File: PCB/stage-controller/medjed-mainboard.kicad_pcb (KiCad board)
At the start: 2 copper layers, 28 parts, among them IC1 TMC429-LI, J1 Barrel_Jack, U1 RP2040

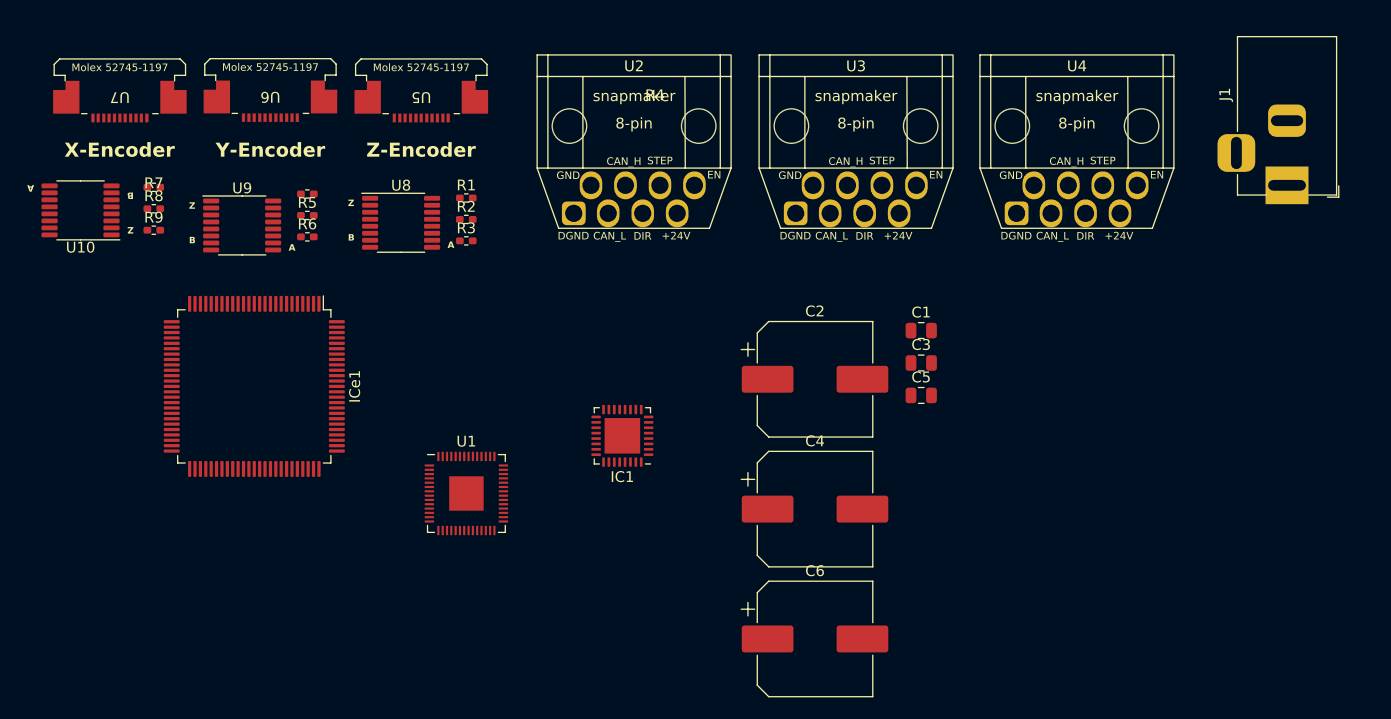
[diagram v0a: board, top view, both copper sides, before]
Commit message: Add initial version stage PCB
Will probably need major revisions as efforts towards TMC4361A will require significant changes.
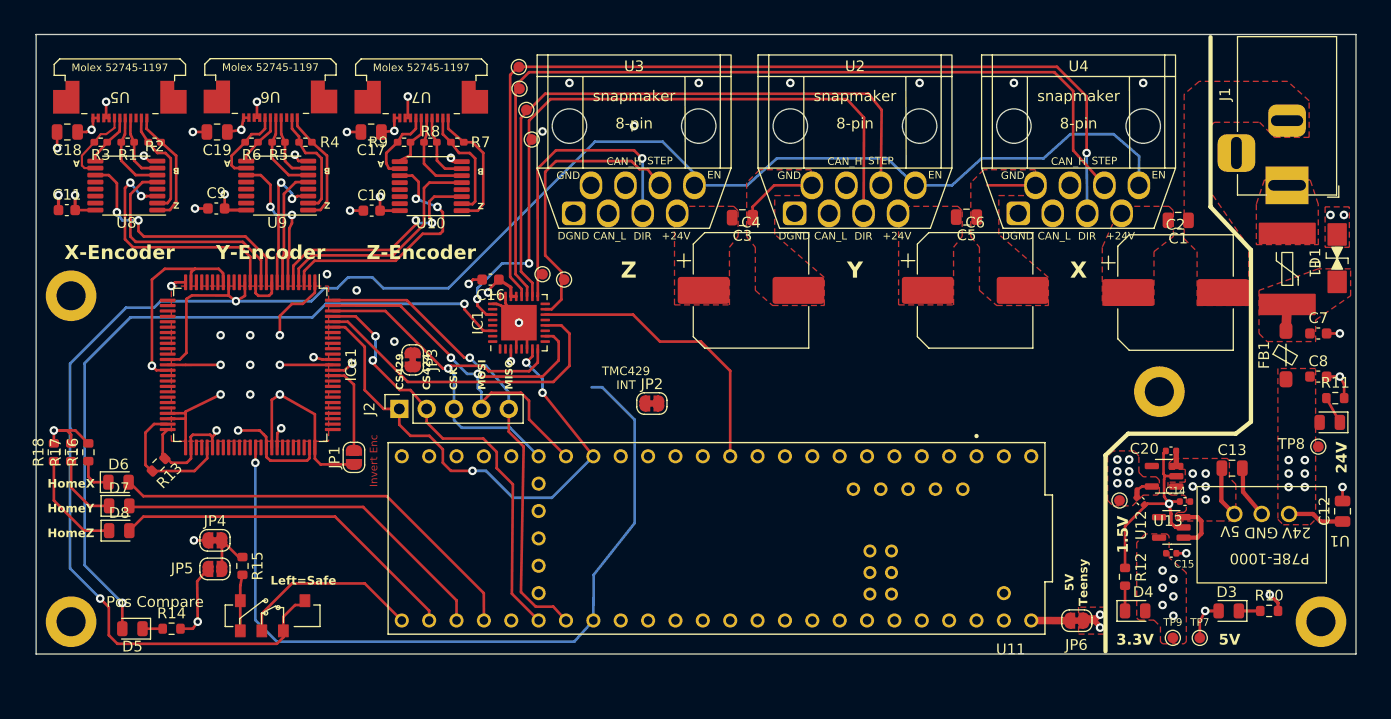
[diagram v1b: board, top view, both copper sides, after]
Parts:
- added ?: , , F.Cu at (135.5, 73.8)
- added ?: , , F.Cu at (120.5, 52.4)
- added ?: , , F.Cu at (19.5, 73.8)
- added C10: 100nF, Capacitor_SMD:C_0603_1608Metric, F.Cu at (47.4, 35.6)
- added C11: 100nF, Capacitor_SMD:C_0603_1608Metric, F.Cu at (19.1, 35.6)
- added C12: 10uF, Capacitor_SMD:C_0805_2012Metric, F.Cu at (137.5, 63.5)
- added C13: 22uF, Capacitor_SMD:C_0805_2012Metric, F.Cu at (127.2, 59.5)
- added C14: 1uF, Capacitor_SMD:C_0402_1005Metric, F.Cu at (122.9, 62.6)
- added C15: 1uF, Capacitor_SMD:C_0402_1005Metric, F.Cu at (121.6, 67.4)
- added C16: 100nF, Capacitor_SMD:C_0603_1608Metric, F.Cu at (58.4, 42.0)
- added C17: 10uF, Capacitor_SMD:C_0805_2012Metric, F.Cu at (47.4, 28.3)
- added C18: 10uF, Capacitor_SMD:C_0805_2012Metric, F.Cu at (19.1, 28.3)
- added C19: 10uF, Capacitor_SMD:C_0805_2012Metric, F.Cu at (33.0, 28.3)
- added C20: 1uF, Capacitor_SMD:C_0402_1005Metric, F.Cu at (121.6, 57.9)
- added C21: 1uF, Capacitor_SMD:C_0402_1005Metric, F.Cu at (118.8, 62.6)
- added C7: 100nF, Capacitor_SMD:C_0603_1608Metric, F.Cu at (135.2, 47.0)
- added C8: 100nF, Capacitor_SMD:C_0603_1608Metric, F.Cu at (135.2, 51.0)
- added C9: 100nF, Capacitor_SMD:C_0603_1608Metric, F.Cu at (33.0, 35.4)
- added D1: SMAJ28CA, medjed-mainboard:SMAJ28CA, F.Cu at (137.0, 40.0)
- added D2: Red, LED_SMD:LED_0805_2012Metric, F.Cu at (136.3, 55.2)
- added D3: Red, LED_SMD:LED_0805_2012Metric, F.Cu at (126.9, 72.8)
- added D4: Red, LED_SMD:LED_0805_2012Metric, F.Cu at (118.2, 72.8)
- added D5: Red, LED_SMD:LED_0805_2012Metric, F.Cu at (25.2, 74.4)
- added D6: Red, LED_SMD:LED_0805_2012Metric, F.Cu at (23.9, 60.8)
- added D7: Red, LED_SMD:LED_0805_2012Metric, F.Cu at (24.0, 63.0)
- added D8: Red, LED_SMD:LED_0805_2012Metric, F.Cu at (24.0, 65.3)
- added F1: SMDC185F/33-2, medjed-mainboard:SMDC185F_33-2, F.Cu at (132.4, 41.0)
- added FB1: FerriteBead, medjed-mainboard:BLM41P600S, F.Cu at (132.2, 49.0)
- added J2: Conn_01x05, Connector_PinSocket_2.54mm:PinSocket_1x05_P2.54mm_Vertical, F.Cu at (50.0, 54.0)
- added JP1: SolderJumper_2_Open, Jumper:SolderJumper-2_P1.3mm_Open_RoundedPad1.0x1.5mm, F.Cu at (45.8, 58.5)
- added JP2: SolderJumper_2_Bridged, Jumper:SolderJumper-2_P1.3mm_Bridged_RoundedPad1.0x1.5mm, F.Cu at (73.4, 53.5)
- added JP3: SolderJumper_2_Bridged, Jumper:SolderJumper-2_P1.3mm_Bridged_RoundedPad1.0x1.5mm, F.Cu at (51.2, 49.5)
- added JP4: SolderJumper_2_Bridged, Jumper:SolderJumper-2_P1.3mm_Bridged_RoundedPad1.0x1.5mm, F.Cu at (32.9, 66.2)
- added JP5: SolderJumper_2_Open, Jumper:SolderJumper-2_P1.3mm_Open_RoundedPad1.0x1.5mm, F.Cu at (32.9, 68.8)
- added JP6: SolderJumper_2_Bridged, Jumper:SolderJumper-2_P1.3mm_Bridged_RoundedPad1.0x1.5mm, F.Cu at (112.8, 73.7)
- added R10: 5k1, Resistor_SMD:R_0603_1608Metric, F.Cu at (130.7, 72.8)
- added R11: 5k1, Resistor_SMD:R_0603_1608Metric, F.Cu at (136.8, 53.0)
- added R12: 5k1, Resistor_SMD:R_0603_1608Metric, F.Cu at (117.3, 69.6)
- added R13: 10k, Resistor_SMD:R_0603_1608Metric, F.Cu at (27.6, 59.2)
- added R14: 5k1, Resistor_SMD:R_0603_1608Metric, F.Cu at (28.8, 74.4)
- added R15: 10k, Resistor_SMD:R_0603_1608Metric, F.Cu at (35.4, 68.6)
- added R16: 5k1, Resistor_SMD:R_0603_1608Metric, F.Cu at (21.1, 58.0)
- added R17: 5k1, Resistor_SMD:R_0603_1608Metric, F.Cu at (19.5, 58.0)
- added R18: 5k1, Resistor_SMD:R_0603_1608Metric, F.Cu at (17.9, 58.0)
- added REF**: MountingHole_2.7mm_M2.5_DIN965_Pad, MountingHole:MountingHole_2.7mm_M2.5_DIN965_Pad, F.Cu at (19.5, 43.5)
- added SW1: SW_Push_SPDT, medjed-mainboard:switch_SS3NP-MS-V-TR, F.Cu at (38.2, 73.2)
- added TP1: TestPoint_Small, TestPoint:TestPoint_Pad_D1.0mm, F.Cu at (61.1, 24.3)
- added TP10: TestPoint, TestPoint:TestPoint_Pad_D1.0mm, F.Cu at (116.8, 62.5)
- added TP2: TestPoint_Small, TestPoint:TestPoint_Pad_D1.0mm, F.Cu at (61.1, 22.3)
- added TP3: TestPoint_Small, TestPoint:TestPoint_Pad_D1.0mm, F.Cu at (61.8, 26.2)
- added TP4: TestPoint_Small, TestPoint:TestPoint_Pad_D1.0mm, F.Cu at (62.2, 29.0)
- added TP5: TestPoint_Small, TestPoint:TestPoint_Pad_D1.0mm, F.Cu at (63.2, 41.5)
- added TP6: TestPoint_Small, TestPoint:TestPoint_Pad_D1.0mm, F.Cu at (65.2, 42.0)
- added TP7: TestPoint, TestPoint:TestPoint_Pad_D1.0mm, F.Cu at (124.2, 75.2)
- added TP8: TestPoint, TestPoint:TestPoint_Pad_D1.0mm, F.Cu at (135.2, 57.5)
- added TP9: TestPoint, TestPoint:TestPoint_Pad_D1.0mm, F.Cu at (121.8, 75.2)
- added U11: teensy 4.1, medjed-mainboard:teensy_4.1, F.Cu at (79.4, 66.0)
- added U12: MIC5317-3.3, Package_TO_SOT_SMD:SOT-23-5, F.Cu at (121.6, 65.0)
- added U13: MIC5317-1.5, Package_TO_SOT_SMD:SOT-23-5, F.Cu at (120.9, 60.2)
- U1: value RP2040 -> P78E-1000; footprint Package_DFN_QFN:QFN-56-1EP_7x7mm_P0.4mm_EP3.2x3.2mm -> medjed-mainboard:P78E-1000
- moved U1 73.8 mm to (130.0, 63.8), turned to 180 degrees
- moved C6 35.6 mm to (103.4, 43.0)
- moved C2 34.4 mm to (122.0, 43.2)
- moved C1 26.0 mm to (122.2, 36.5), turned to 180 degrees
- moved C3 21.4 mm to (81.8, 36.2), turned to 180 degrees
- moved C4 21.2 mm to (82.6, 43.0)
- moved U4 20.7 mm to (113.0, 31.6)
- moved U2 20.6 mm to (92.2, 31.6)
- moved C5 17.1 mm to (102.6, 36.2), turned to 180 degrees
- moved IC1 14.2 mm to (61.1, 46.0), turned to 90 degrees
- moved R9 10.8 mm to (50.4, 29.2), turned to 180 degrees
- moved R6 10.2 mm to (36.2, 29.2), turned to 180 degrees
- moved R3 9.54 mm to (22.2, 29.2), turned to 180 degrees
- moved R5 7.30 mm to (38.8, 29.2), turned to 180 degrees
- moved R7 7.21 mm to (55.3, 29.2), turned to 180 degrees
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- renumbered R8 to R1, R7 to R2, R9 to R3, R2 to R7, R1 to R8, R3 to R9, U8 to U10, U4 to U2, U2 to U3, U3 to U4, U7 to U5, U5 to U7, U10 to U8
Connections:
- net Net-(IC1-SCK_C) renamed SCK
- net Net-(IC1-SDI_C) renamed MOSI
- net Net-(IC1-SDOZ_C) renamed /SDO-429
- net Net-(IC1-~{SCS_C}) renamed CS429
- net Net-(ICe1-ENC1_A) renamed /ENC_A_Z
- net Net-(ICe1-ENC1_B) renamed /ENC_B_Z
- net Net-(ICe1-ENC1_N) renamed /ENC_N_Z
- net Net-(ICe1-ENC2_A) renamed /ENC_A_Y
- net Net-(ICe1-ENC2_B) renamed /ENC_B_Y
- net Net-(ICe1-ENC2_N) renamed /ENC_N_Y
- net Net-(ICe1-ENC3_A) renamed /ENC_A_X
- net Net-(ICe1-ENC3_B) renamed /ENC_B_X
- net Net-(ICe1-ENC3_N) renamed /ENC_N_X
- net Net-(U10-1A) renamed /X_Z+
- net Net-(U10-1B) renamed /X_Z-
- net Net-(U10-2A) renamed /X_B+
- net Net-(U10-2B) renamed /X_B-
- net Net-(U10-3A) renamed /X_A+
- net Net-(U10-3B) renamed /X_A-
- net Net-(U5-A+) renamed /Z_A+
- net Net-(U5-A-) renamed /Z_A-
- net Net-(U5-B+) renamed /Z_B+
- net Net-(U5-B-) renamed /Z_B-
- net Net-(U5-Z+) renamed /Z_Z+
- net Net-(U5-Z-) renamed /Z_Z-
- net Net-(U6-A+) renamed /Y_A+
- net Net-(U6-A-) renamed /Y_A-
- net Net-(U6-B+) renamed /Y_B+
- net Net-(U6-B-) renamed /Y_B-
- net Net-(U6-Z+) renamed /Y_Z+
- net Net-(U6-Z-) renamed /Y_Z-
- C1 pad 2: Net-(U4-+24V) -> +24V
- C2 pad 1: Net-(U4-+24V) -> +24V
- C3 pad 2: Net-(U2-+24V) -> +24V
- C4 pad 1: Net-(U2-+24V) -> +24V
- C5 pad 2: Net-(U3-+24V) -> +24V
- C6 pad 1: Net-(U3-+24V) -> +24V
- IC1 pad 14: unconnected-(IC1-~{INT_SDO_C}-Pad14) -> INT_429
- IC1 pad 15: Net-(IC1-SDO_S_S1) -> /STEP-Z
- IC1 pad 17: Net-(IC1-SCK_S_D1) -> /DIR-Z
- IC1 pad 18: Net-(IC1-~{SCS_S_S2}) -> /STEP-Y
- IC1 pad 19: Net-(IC1-~{SCS2_S3}) -> /STEP-X
- IC1 pad 20: Net-(IC1-~{SCS3_D3}) -> /DIR-X
- IC1 pad 21: unconnected-(IC1-V5@2-Pad21) -> +3.3V
- IC1 pad 22: unconnected-(IC1-V33-Pad22) -> +3.3V
- IC1 pad 27: Net-(IC1-SDI_S_D2) -> /DIR-Y
- IC1 pad 3: unconnected-(IC1-V5@1-Pad3) -> +3.3V
- IC1 pad 30: unconnected-(IC1-POSCMP-Pad30) -> /POSCMP
- IC1 pad 33: (no net) -> GND
- IC1 pad 5: unconnected-(IC1-CLK-Pad5) -> TeensyCLK
- ICe1 pad 1: unconnected-(ICe1-GND@1-Pad1) -> GND
- ICe1 pad 100: unconnected-(ICe1-SDO-Pad100) -> MISO
- ICe1 pad 12: unconnected-(ICe1-GND@3-Pad12) -> GND
- ICe1 pad 14: unconnected-(ICe1-VCORE@1-Pad14) -> +1V5
- ICe1 pad 17: unconnected-(ICe1-VCORE@2-Pad17) -> +1V5
- ICe1 pad 18: unconnected-(ICe1-VCCI@1-Pad18) -> +3.3V
- ICe1 pad 24: unconnected-(ICe1-VCC@1-Pad24) -> +3.3V
- ICe1 pad 25: unconnected-(ICe1-GND@4-Pad25) -> GND
- ICe1 pad 37: unconnected-(ICe1-VCORE@3-Pad37) -> +1V5
- ICe1 pad 38: unconnected-(ICe1-GND@5-Pad38) -> GND
- ICe1 pad 39: unconnected-(ICe1-VCCI@2-Pad39) -> +3.3V
- ICe1 pad 47: unconnected-(ICe1-TCK-Pad47) -> GND
- ICe1 pad 48: unconnected-(ICe1-TDI-Pad48) -> GND
- ICe1 pad 49: unconnected-(ICe1-TMS-Pad49) -> Net-(ICe1-TMS)
- ICe1 pad 50: unconnected-(ICe1-VCC@2-Pad50) -> +3.3V
- ICe1 pad 51: unconnected-(ICe1-GND@6-Pad51) -> GND
- ICe1 pad 52: unconnected-(ICe1-VCC@3-Pad52) -> +3.3V
- ICe1 pad 55: unconnected-(ICe1-TRST-Pad55) -> Net-(ICe1-TMS)
- ICe1 pad 56: unconnected-(ICe1-VCC@4-Pad56) -> +3.3V
- ICe1 pad 64: unconnected-(ICe1-CLK-Pad64) -> TeensyCLK
- ICe1 pad 66: unconnected-(ICe1-VCCI@3-Pad66) -> +3.3V
- ICe1 pad 67: unconnected-(ICe1-GND@7-Pad67) -> GND
- ICe1 pad 68: unconnected-(ICe1-VCORE@4-Pad68) -> +1V5
- ICe1 pad 74: unconnected-(ICe1-VCC@5-Pad74) -> +3.3V
- ICe1 pad 75: unconnected-(ICe1-GND@8-Pad75) -> GND
- ICe1 pad 86: unconnected-(ICe1-ENC_INV-Pad86) -> Net-(ICe1-ENC_INV)
- ICe1 pad 87: unconnected-(ICe1-VCCI@4-Pad87) -> +3.3V
- ICe1 pad 88: unconnected-(ICe1-GND@9-Pad88) -> GND
- ICe1 pad 89: unconnected-(ICe1-VCORE@5-Pad89) -> +1V5
- ICe1 pad 9: unconnected-(ICe1-GND@2-Pad9) -> GND
- ICe1 pad 92: unconnected-(ICe1-EXT_RES-Pad92) -> Net-(ICe1-EXT_RES)
- ICe1 pad 94: unconnected-(ICe1-~{INT}-Pad94) -> INT_424
- ICe1 pad 97: unconnected-(ICe1-~{SCS}-Pad97) -> CS424
- J1 pad 1: unconnected-(J1-Pad1) -> /+24Vsrc
- J1 pad 2: unconnected-(J1-Pad2) -> GND
- U1 pad 1: Net-(U1-IOVDD-Pad1) -> +24V
- U1 pad 2: unconnected-(U1-GPIO0-Pad2) -> GND
- U1 pad 3: unconnected-(U1-GPIO1-Pad3) -> +5V
- U10 pad 16: /+5V -> +5V
- U2 pad 5: Net-(IC1-~{SCS3_D3}) -> /DIR-Y
- U2 pad 6: Net-(IC1-~{SCS2_S3}) -> /STEP-Y
- U2 pad 7: Net-(U4-+24V) -> +24V
- U3 pad 5: Net-(IC1-SDI_S_D2) -> /DIR-Z
- U3 pad 6: Net-(IC1-~{SCS_S_S2}) -> /STEP-Z
- U3 pad 7: Net-(U2-+24V) -> +24V
- U4 pad 5: Net-(IC1-SCK_S_D1) -> /DIR-X
- U4 pad 6: Net-(IC1-SDO_S_S1) -> /STEP-X
- U4 pad 7: Net-(U3-+24V) -> +24V
- U5 pad 1: /+5V -> +5V
- U5 pad 2: /+5V -> +5V
- U5 pad 4: unconnected-(U7-GND-Pad4) -> GND
- U6 pad 1: /+5V -> +5V
- U6 pad 2: /+5V -> +5V
- U7 pad 1: /+5V -> +5V
- U7 pad 2: /+5V -> +5V
- U8 pad 16: /+5V -> +5V
- U9 pad 16: /+5V -> +5V
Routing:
- net +1V5: track 0.00 -> 302.3 mm, vias 0 -> 10
- net GND: track 0.00 -> 139.7 mm, vias 0 -> 45
- net +3.3V: track 0.00 -> 87.0 mm, vias 0 -> 13
- net /DIR-X: track 0.00 -> 86.8 mm, vias 0 -> 1
- net /STEP-X: track 0.00 -> 82.8 mm
- net TeensyCLK: track 0.00 -> 74.3 mm, vias 0 -> 1
- net +5V: track 0.00 -> 68.8 mm, vias 0 -> 14
- net /POSCMP: track 0.00 -> 67.6 mm, vias 0 -> 2
- net /DIR-Y: track 0.00 -> 63.9 mm, vias 0 -> 2
- net /STEP-Y: track 0.00 -> 59.1 mm
- net CS429: track 0.00 -> 49.0 mm, vias 0 -> 3
- net MISO: track 0.00 -> 44.4 mm, vias 0 -> 1
- net MOSI: track 0.00 -> 43.3 mm, vias 0 -> 2
- net CS424: track 0.00 -> 40.6 mm, vias 0 -> 2
- net HomeX: track 0.00 -> 39.8 mm
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- added copper zone on F.Cu, net +1V5
- added copper zone on In2.Cu, net +1V5
- added copper zone on F.Cu, net +24V
- added copper zone on In2.Cu, net +24V
- added copper zone on F.Cu, net +3.3V
- added copper zone on In2.Cu, net +3.3V
- added copper zone on F.Cu, net +5V
- added copper zone on In2.Cu, net +5V
- added copper zone on F.Cu, net /+24Vfused
- added copper zone on F.Cu, net /+24Vsrc
- added copper zone on F.Cu, net GND
- added copper zone on In1.Cu, net GND
- added copper zone on In2.Cu, net GND
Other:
- board outline added: 122.5 x 57.5 mm
- copper layers 2 -> 4
- board text added: "1.5V"
- board text added: "24V"
- board text added: "3.3V"
- board text added: "5V"
- board text added: "5V Teensy"
- board text added: "CS424"
- board text added: "CS429"
- board text added: "CSK"
- board text added: "HomeX"
- board text added: "HomeY"
- board text added: "HomeZ"
- board text added: "Invert Enc"
- board text added: "Left=Safe"
- board text added: "MISO"
- board text added: "MOSI"
- board text added: "Pos Compare"
- board text added: "TMC429 INT"
- board text added: "X"
- board text added: "Y"
- board text added: "Z"

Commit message: New TMC4361 design
Redesigned stage controller around the TMC4361.
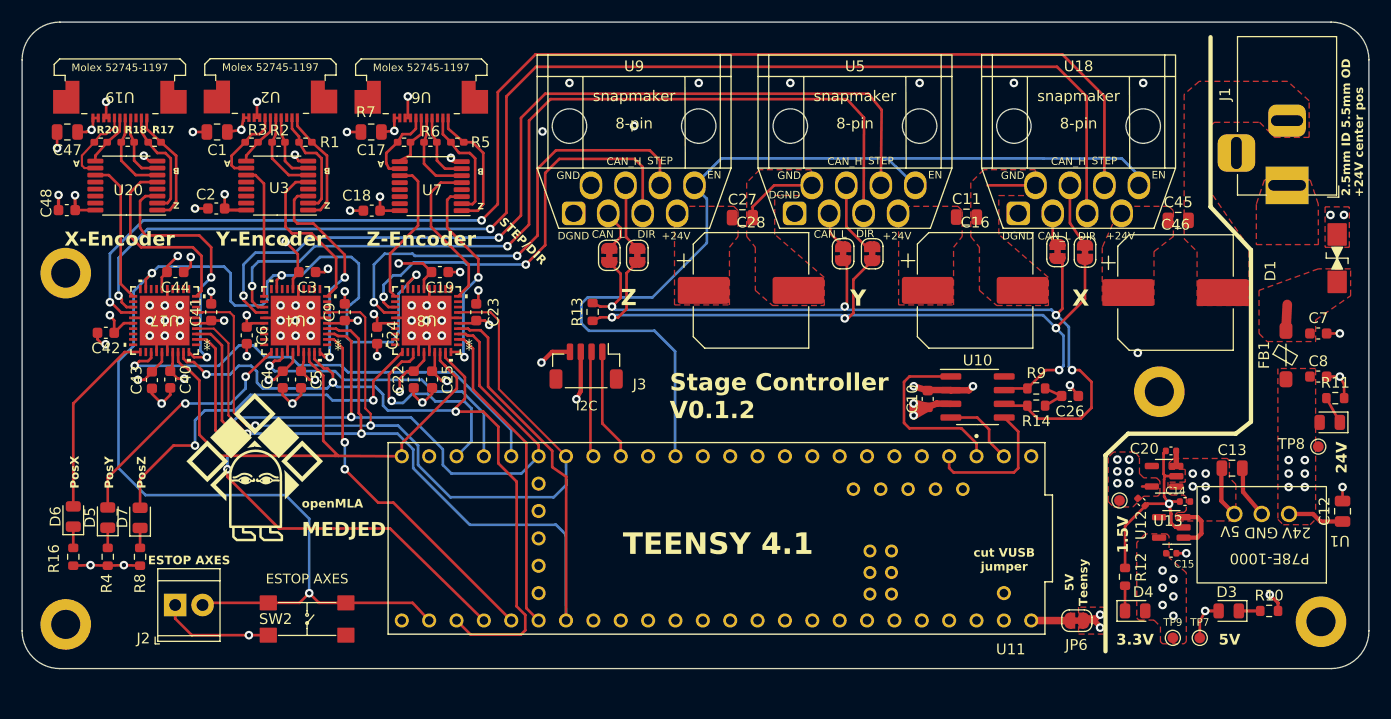
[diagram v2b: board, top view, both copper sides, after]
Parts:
- removed the C16 at (58.4, 42.0)
- removed D8: Red, LED_SMD:LED_0805_2012Metric
- removed F1: SMDC185F/33-2, medjed-mainboard:SMDC185F_33-2
- removed IC1: TMC429-LI, Package_DFN_QFN:QFN-32-1EP_5x5mm_P0.5mm_EP3.3x3.3mm
- removed ICe1: TMC424, Package_QFP:TQFP-100_14x14mm_P0.5mm
- removed R15: 10k, Resistor_SMD:R_0603_1608Metric
- removed the R17 at (19.5, 58.0)
- removed the R18 at (17.9, 58.0)
- removed SW1: SW_Push_SPDT, medjed-mainboard:switch_SS3NP-MS-V-TR
- removed TP1, TP2, TP3, TP4, TP5, TP6: TestPoint_Small, TestPoint:TestPoint_Pad_D1.0mm
- added C10: 100nF, Capacitor_SMD:C_0603_1608Metric, F.Cu at (99.0, 53.1)
- added C19: 100nF, Capacitor_SMD:C_0603_1608Metric, F.Cu at (53.7, 41.3)
- added C22: 100nF, Capacitor_SMD:C_0603_1608Metric, F.Cu at (51.3, 51.3)
- added C23: 100nF, Capacitor_SMD:C_0603_1608Metric, F.Cu at (57.1, 45.0)
- added C24: 100nF, Capacitor_SMD:C_0603_1608Metric, F.Cu at (47.9, 47.2)
- added C25: 100nF, Capacitor_SMD:C_0603_1608Metric, F.Cu at (53.0, 51.3)
- added C26: 4.7nF, Capacitor_SMD:C_0603_1608Metric, F.Cu at (112.2, 52.8)
- added C3: 100nF, Capacitor_SMD:C_0603_1608Metric, F.Cu at (41.4, 41.3)
- added C4: 100nF, Capacitor_SMD:C_0603_1608Metric, F.Cu at (39.1, 51.3)
- added C40: 100nF, Capacitor_SMD:C_0603_1608Metric, F.Cu at (28.7, 51.3)
- added C41: 100nF, Capacitor_SMD:C_0603_1608Metric, F.Cu at (32.5, 45.0)
- added C42: 100nF, Capacitor_SMD:C_0603_1608Metric, F.Cu at (22.7, 46.9)
- added C43: 100nF, Capacitor_SMD:C_0603_1608Metric, F.Cu at (27.0, 51.3)
- added C44: 100nF, Capacitor_SMD:C_0603_1608Metric, F.Cu at (29.2, 41.3)
- added C5: 100nF, Capacitor_SMD:C_0603_1608Metric, F.Cu at (40.8, 51.3)
- added C6: 100nF, Capacitor_SMD:C_0603_1608Metric, F.Cu at (35.8, 47.2)
- added C9: 100nF, Capacitor_SMD:C_0603_1608Metric, F.Cu at (44.9, 45.0)
- added G***: LOGO, medjed-mainboard:MEDJED-logo-15mm, F.Cu at (36.5, 59.5)
- added G***: LOGO, medjed-mainboard:open-MLA-logo, B.Cu at (64.2, 57.9)
- added J3: Conn_01x04_Pin, Connector_JST:JST_SH_BM04B-SRSS-TB_1x04-1MP_P1.00mm_Vertical, F.Cu at (67.3, 50.0)
- added JP7: SolderJumper_2_Bridged, Jumper:SolderJumper-2_P1.3mm_Bridged_RoundedPad1.0x1.5mm, F.Cu at (111.0, 39.4)
- added R4: 5k1, Resistor_SMD:R_0603_1608Metric, F.Cu at (22.9, 67.7)
- added R8: 5k1, Resistor_SMD:R_0603_1608Metric, F.Cu at (25.9, 67.7)
- added R9: 60, Resistor_SMD:R_0603_1608Metric, F.Cu at (109.1, 52.1)
- added SW2: ESTOP switch, medjed-mainboard:E-switch-button, F.Cu at (41.4, 73.5)
- added U10: TCAN330, Package_SO:SOIC-8_3.9x4.9mm_P1.27mm, F.Cu at (103.6, 52.9)
- added U17: TMC4361A-LA, medjed-mainboard:TMC4361A_QFN40_6X6_TRI, F.Cu at (28.2, 45.8)
- added U4: TMC4361A-LA, medjed-mainboard:TMC4361A_QFN40_6X6_TRI, F.Cu at (40.3, 45.8)
- added U8: TMC4361A-LA, medjed-mainboard:TMC4361A_QFN40_6X6_TRI, F.Cu at (52.5, 45.8)
- J2: value Conn_01x05 -> ESTOP terminal; footprint Connector_PinSocket_2.54mm:PinSocket_1x05_P2.54mm_Vertical -> TerminalBlock_TE-Connectivity:TerminalBlock_TE_282834-2_1x02_P2.54mm_Horizontal
- JP1, JP5: value SolderJumper_2_Open -> SolderJumper_2_Bridged; footprint Jumper:SolderJumper-2_P1.3mm_Open_RoundedPad1.0x1.5mm -> Jumper:SolderJumper-2_P1.3mm_Bridged_RoundedPad1.0x1.5mm
- R13: value 10k -> 120
- R14: value 5k1 -> 60
- U13: value MIC5317-1.5 -> MIC5317-1.8
- moved JP5 85.9 mm to (113.6, 39.5), turned to -90 degrees
- moved R14 82.9 mm to (109.1, 53.7), turned to 180 degrees
- moved JP4 66.5 mm to (93.8, 39.6), turned to -90 degrees
- moved R13 42.7 mm to (67.9, 45.0), turned to 90 degrees
- moved JP3 41.1 mm to (91.2, 39.6)
- moved JP1 32.3 mm to (72.0, 39.8), turned to -90 degrees
- moved J2 27.6 mm to (29.2, 72.2), turned to 0 degrees
- moved JP2 14.3 mm to (69.5, 39.8), turned to -90 degrees
- moved D5 10.6 mm to (22.9, 64.1), turned to 90 degrees
- moved R16 9.80 mm to (19.7, 67.7), turned to -90 degrees
- moved D6 5.27 mm to (19.7, 64.0), turned to 90 degrees
- moved D7 2.23 mm to (25.9, 64.1), turned to 90 degrees
- moved REF** 2.18 mm to (18.9, 41.4)
- moved C21 0.11 mm to (118.8, 62.6)
- turned C11 to 0 degrees
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- renumbered C19 to C1, C5 to C11, C6 to C16, C10 to C18, C9 to C2, C3 to C27, C4 to C28, C1 to C45, C2 to C46, C18 to C47, C11 to C48, R4 to R1, R2 to R17, R1 to R18, R5 to R2, R3 to R20, R6 to R3, R7 to R5, R8 to R6, R9 to R7, U4 to U18, U5 to U19, U6 to U2, U8 to U20, U9 to U3, U2 to U5, U7 to U6, U10 to U7, U3 to U9
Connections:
- net +1V5 renamed +1V8
- net /X_A+ renamed /Axis X/Z_A+
- net /X_A- renamed /Axis X/Z_A-
- net /X_B+ renamed /Axis X/Z_B+
- net /X_B- renamed /Axis X/Z_B-
- net /X_Z+ renamed /Axis X/Z_Z+
- net /X_Z- renamed /Axis X/Z_Z-
- net /Y_A+ renamed /Axis Y/Z_A+
- net /Y_A- renamed /Axis Y/Z_A-
- net /Y_B+ renamed /Axis Y/Z_B+
- net /Y_B- renamed /Axis Y/Z_B-
- net /Y_Z+ renamed /Axis Y/Z_Z+
- net /Y_Z- renamed /Axis Y/Z_Z-
- net /Z_A+ renamed /Axis Z/Z_A+
- net /Z_A- renamed /Axis Z/Z_A-
- net /Z_B+ renamed /Axis Z/Z_B+
- net /Z_B- renamed /Axis Z/Z_B-
- net /Z_Z+ renamed /Axis Z/Z_Z+
- net /Z_Z- renamed /Axis Z/Z_Z-
- C11 pad 1: GND -> +24V
- C11 pad 2: +24V -> GND
- C18 pad 1: GND -> +5V
- C18 pad 2: +5V -> GND
- C2 pad 1: GND -> +5V
- C2 pad 2: +5V -> GND
- C27 pad 1: GND -> +24V
- C27 pad 2: +24V -> GND
- C45 pad 1: GND -> +24V
- C45 pad 2: +24V -> GND
- C48 pad 1: GND -> +5V
- C48 pad 2: +5V -> GND
- D5 pad 2: /POSCMP -> /Axis Y/TGT
- D6 pad 2: HomeX -> /Axis X/TGT
- D7 pad 2: HomeY -> /Axis Z/TGT
- J2 pad 1: CS429 -> GND
- J2 pad 2: CS424 -> SAFETY
- JP1 pad 1: GND -> /Axis Z/CAN_H
- JP1 pad 2: Net-(ICe1-ENC_INV) -> CAN_H
- JP2 pad 1: /SDO-429 -> /Axis Z/CAN_L
- JP2 pad 2: MISO -> CAN_L
- JP3 pad 1: Net-(ICe1-EXT_RES) -> /Axis Y/CAN_L
- JP3 pad 2: +3.3V -> CAN_L
- JP4 pad 1: +3.3V -> /Axis Y/CAN_H
- JP4 pad 2: /STEP_EN_MANUAL -> CAN_H
- JP5 pad 1: GND -> /Axis X/CAN_H
- JP5 pad 2: /STEP_EN_MANUAL -> CAN_H
- R13 pad 1: +3.3V -> CAN_H
- R13 pad 2: Net-(ICe1-TMS) -> CAN_L
- R14 pad 1: Net-(D5-K) -> Net-(C26-Pad2)
- R14 pad 2: GND -> CAN_L
- U11 pad 0: unconnected-(U11-RX1-Pad0) -> Net-(U10-RXD)
- U11 pad 1: unconnected-(U11-TX1-Pad1) -> Net-(U10-TXD)
- U11 pad 10: INT_429 -> unconnected-(U11-CS1-Pad10)
- U11 pad 12: unconnected-(U11-MISO-Pad12) -> EN_SNAP
- U11 pad 16: INT_424 -> unconnected-(U11-A2-Pad16)
- U11 pad 2: unconnected-(U11-OUT2-Pad2) -> CAN_EN
- U11 pad 24: unconnected-(U11-A10-Pad24) -> /SCL
- U11 pad 25: CS429 -> /SDA
- U11 pad 28: unconnected-(U11-RX7-Pad28) -> INT_X
- U11 pad 29: unconnected-(U11-TX7-Pad29) -> INT_Y
- U11 pad 30: unconnected-(U11-CRX3-Pad30) -> INT_Z
- U11 pad 32: unconnected-(U11-OUT1B-Pad32) -> TeensyCLK
- U11 pad 33: STEPPER_EN -> unconnected-(U11-MCLK2-Pad33)
- U11 pad 34: HomeZ -> SAFETY
- U11 pad 35: HomeY -> RST_AXES
- U11 pad 36: HomeX -> CS_X
- U11 pad 37: unconnected-(U11-CS3-Pad37) -> CS_Y
- U11 pad 38: CS424 -> CS_Z
- U11 pad 40: TeensyCLK -> unconnected-(U11-A16-Pad40)
- U18 pad 1: unconnected-(U4-DGND-Pad1) -> GND
- U18 pad 3: unconnected-(U4-CAN_L-Pad3) -> /Axis X/CAN_L
- U18 pad 4: unconnected-(U4-CAN_H-Pad4) -> /Axis X/CAN_H
- U18 pad 5: /DIR-X -> /Axis X/DIR
- U18 pad 6: /STEP-X -> /Axis X/STEP
- U18 pad 8: /EN motors -> EN_SNAP
- U20 pad 11: /ENC_A_X -> /Axis X/N
- U20 pad 3: /ENC_N_X -> /Axis X/A
- U20 pad 5: /ENC_B_X -> /Axis X/B
- U3 pad 11: /ENC_A_Y -> /Axis Y/N
- U3 pad 3: /ENC_N_Y -> /Axis Y/A
- U3 pad 5: /ENC_B_Y -> /Axis Y/B
- U5 pad 1: unconnected-(U2-DGND-Pad1) -> GND
- U5 pad 3: unconnected-(U2-CAN_L-Pad3) -> /Axis Y/CAN_L
- U5 pad 4: unconnected-(U2-CAN_H-Pad4) -> /Axis Y/CAN_H
- U5 pad 5: /DIR-Y -> /Axis Y/DIR
- U5 pad 6: /STEP-Y -> /Axis Y/STEP
- U5 pad 8: /EN motors -> EN_SNAP
- U7 pad 11: /ENC_A_Z -> /Axis Z/N
- U7 pad 3: /ENC_N_Z -> /Axis Z/A
- U7 pad 5: /ENC_B_Z -> /Axis Z/B
- U9 pad 1: unconnected-(U3-DGND-Pad1) -> GND
- U9 pad 3: unconnected-(U3-CAN_L-Pad3) -> /Axis Z/CAN_L
- U9 pad 4: unconnected-(U3-CAN_H-Pad4) -> /Axis Z/CAN_H
- U9 pad 5: /DIR-Z -> /Axis Z/DIR
- U9 pad 6: /STEP-Z -> /Axis Z/STEP
- U9 pad 8: /EN motors -> EN_SNAP
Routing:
- net +1V8: track 302.3 -> 77.6 mm, vias 10 -> 12
- net /Axis X/STEP: track 0.00 -> 123.1 mm, vias 0 -> 2
- net /Axis X/DIR: track 0.00 -> 121.0 mm, vias 0 -> 2
- net SAFETY: track 0.00 -> 117.7 mm, vias 0 -> 4
- net EN_SNAP: track 0.00 -> 88.7 mm
- net /DIR-X: track 86.8 -> 0.00 mm, vias 1 -> 0
- net /Axis Y/STEP: track 0.00 -> 84.5 mm, vias 0 -> 2
- net /Axis Y/DIR: track 0.00 -> 83.0 mm, vias 0 -> 2
- net /STEP-X: track 82.8 -> 0.00 mm
- net CAN_L: track 0.00 -> 78.3 mm, vias 0 -> 4
- net CAN_H: track 0.00 -> 74.6 mm, vias 0 -> 4
- net RST_AXES: track 0.00 -> 72.2 mm, vias 0 -> 3
- net /POSCMP: track 67.6 -> 0.00 mm, vias 2 -> 0
- net /DIR-Y: track 63.9 -> 0.00 mm, vias 2 -> 0
- net /STEP-Y: track 59.1 -> 0.00 mm
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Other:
- board size 122.5 x 57.5 mm -> 125 x 60 mm
- board text added: "+24V center pos"
- board text added: "2.5mm ID 5.5mm OD"
- board text added: "ESTOP AXES"
- board text added: "I2C"
- board text added: "MEDJED"
- board text added: "PosX"
- board text added: "PosY"
- board text added: "PosZ"
- board text added: "STEP/DIR"
- board text added: "Stage Controller V0.1.2"
- board text added: "TEENSY 4.1"
- board text added: "cut VUSB jumper"
- board text added: "openMLA"
- board text removed: "CS424"
- board text removed: "CS429"
- board text removed: "CSK"
- board text removed: "HomeX"
- board text removed: "HomeY"
- board text removed: "HomeZ"
- board text removed: "Invert Enc"
- board text removed: "Left=Safe"
- board text removed: "MISO"
- board text removed: "MOSI"
- board text removed: "Pos Compare"
- board text removed: "TMC429 INT"

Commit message: Finalise part numbers and I2C pullup
Complete mouser part numbers. Added pullup for I2C connector.
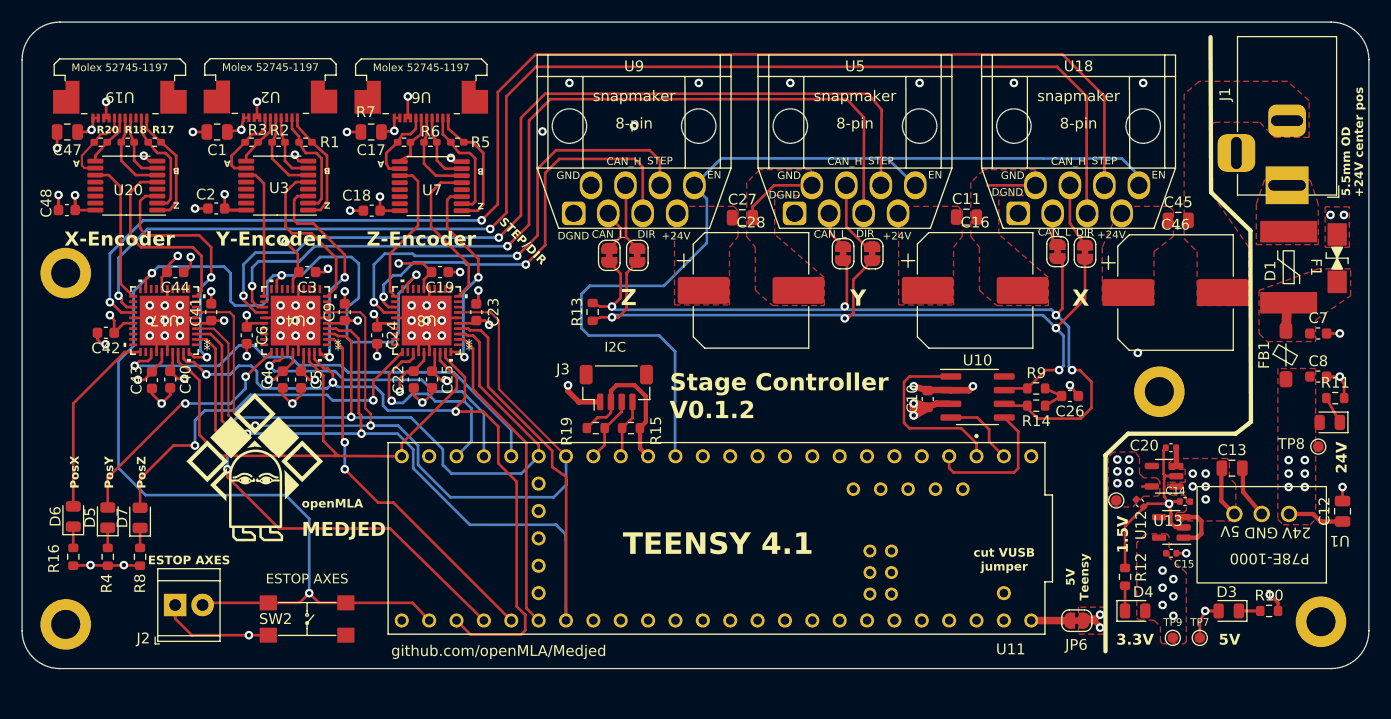
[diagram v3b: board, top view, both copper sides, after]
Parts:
- added F1: SMDC185F/33-2, medjed-mainboard:SMDC185F_33-2, F.Cu at (132.5, 40.9)
- added R15: 5k1, Resistor_SMD:R_0603_1608Metric, F.Cu at (71.5, 55.8)
- added R19: 5k1, Resistor_SMD:R_0603_1608Metric, F.Cu at (68.2, 55.8)
- R14, R9: value 60 -> 60.4
- moved J3 3.44 mm to (70.1, 52.0), turned to 0 degrees
- moved C20 0.30 mm to (121.6, 57.6)
- moved TP10 0.30 mm to (116.5, 62.5)
- moved C21 0.18 mm to (118.7, 62.8)
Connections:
- net SAFETY renamed ESTOP
- J3 pad 1: /SCL -> GND
- J3 pad 2: /SDA -> /+3.3V Teensy
- J3 pad 3: +3.3V -> /SDA
- J3 pad 4: GND -> /SCL
- U11 pad 3.3V_1: Net-(U11-3.3V-Pad3.3V_1) -> /+3.3V Teensy
- U11 pad 3.3V_2: Net-(U11-3.3V-Pad3.3V_1) -> /+3.3V Teensy
- U11 pad 3.3V_3: Net-(U11-3.3V-Pad3.3V_1) -> /+3.3V Teensy
- U11 pad USB_GND1: Net-(U11-USB_GND-PadUSB_GND1) -> unconnected-(U11-USB_GND-PadUSB_GND1)
- U11 pad USB_GND2: Net-(U11-USB_GND-PadUSB_GND1) -> unconnected-(U11-USB_GND-PadUSB_GND1)
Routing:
- net /+3.3V Teensy: track 0.00 -> 14.8 mm
- net /SCL: track 10.4 -> 5.65 mm
- net +3.3V: track 39.7 -> 35.2 mm, vias 18 -> 17
- net /SDA: track 9.85 -> 6.55 mm
- net GND: track 163.5 -> 164.7 mm
- net EN_SNAP: track 88.7 -> 89.5 mm
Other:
- board text added: "5.5mm OD"
- board text added: "github.com/openMLA/Medjed"
- board text removed: "2.5mm ID 5.5mm OD"
